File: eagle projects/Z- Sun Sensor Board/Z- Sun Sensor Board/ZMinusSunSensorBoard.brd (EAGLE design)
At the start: 78 x 78 mm, 53 parts, among them U2 ADS7841E_2K5, U4 LM20BIM7X_NOPB, U6 TLV9051IDCKR, U8 TLV9051IDCKR, U9 TLV9051IDCKR

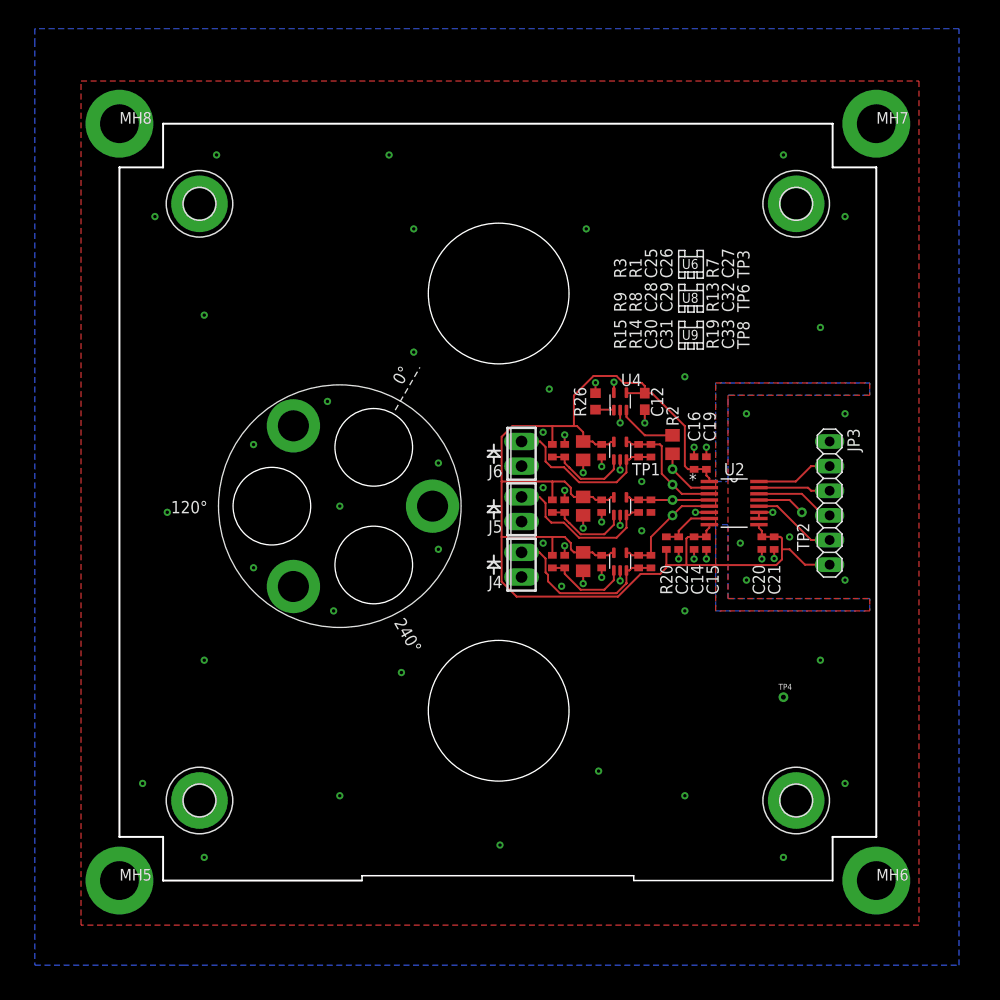
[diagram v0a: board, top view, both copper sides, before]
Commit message: Added mounting holes for sun sensor board, added standoff mounting holes to sensor board
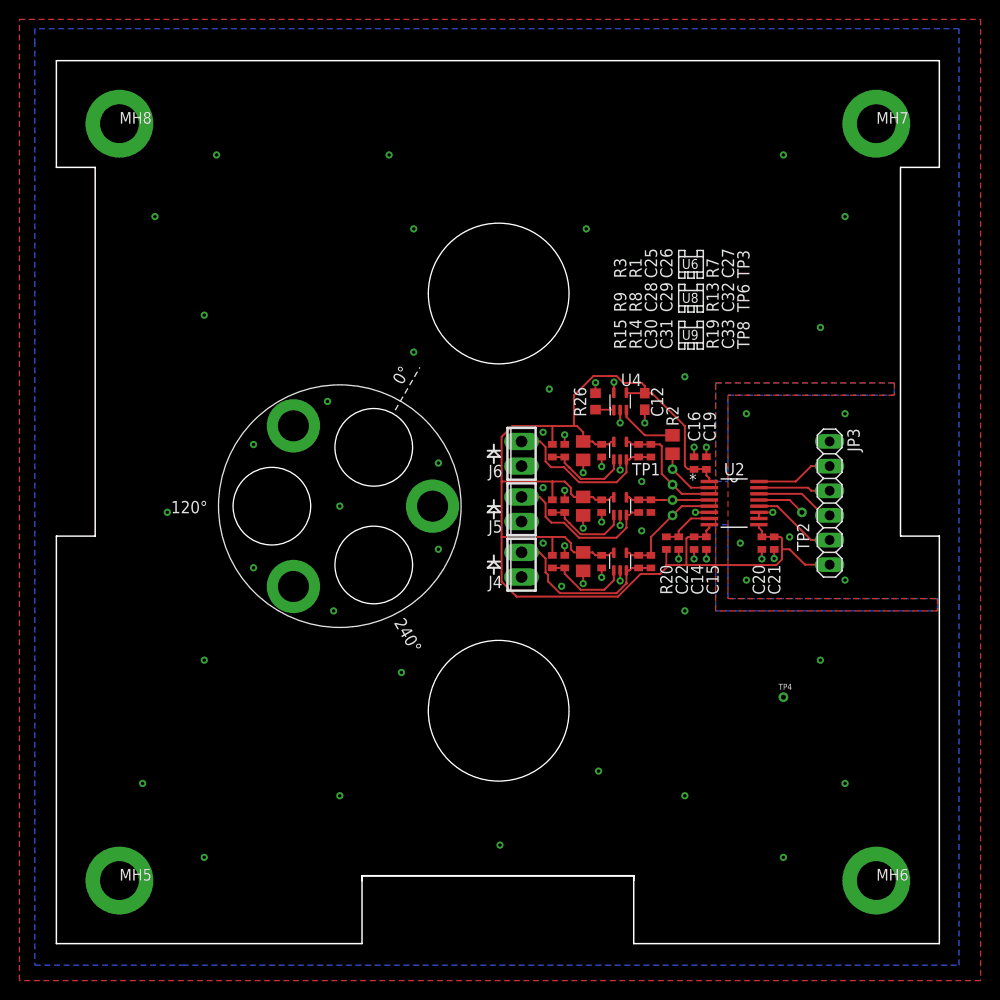
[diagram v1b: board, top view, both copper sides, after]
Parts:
- removed H1, H2, H3, H4: MOUNT-PAD-ROUND3.2, holes:3,2-PAD
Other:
- board size 78 x 78 mm -> 91 x 91 mm
- board text added: "Z- SUN SENSOR BOARD - Rev A"
- board text removed: "Z+ SUN SENSOR BOARD - Rev A"
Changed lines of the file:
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@@
 <setting verticaltext="up"/>
 </settings>
-<grid distance="25" unitdist="mil" unit="mil" style="lines" multiple="1" display="yes" altdistance="12.5" altunitdist="mil" altunit="mil"/>
+<grid distance="25" unitdist="mil" unit="mm" style="lines" multiple="1" display="yes" altdistance="12.5" altunitdist="mil" altunit="mil"/>
 <layers>
 <layer number="1" name="Top" color="4" fill="1" visible="yes" active="yes"/>
@@
 </layers>
 <board>
-<fusionsync huburn="a.YnVzaW5lc3M6bXlkYWwyMA" projecturn="a.YnVzaW5lc3M6bXlkYWwyMCMyMDE5MDkwNjIxMzMzMjg1MQ" f3durn="urn:adsk.wipprod:dm.lineage:9eKYqUHQRJ-z_v29RI24zA" pcbguid="" lastpulledtime="" lastsyncedchangeguid="" latestrevisionid="e225897c-414a-45e0-9606-f7f44216a340" lastsyncedrevisionid="e225897c-414a-45e0-9606-f7f44216a340" lastboardhashguid="898b3bb0-e8cf-4f41-3e9a-b056dcb77d80" lastpushedtime="2020-10-26T20:08:05Z" linktopcb3d="true"/>
+<fusionsync huburn="a.YnVzaW5lc3M6bXlkYWwyMA" projecturn="a.YnVzaW5lc3M6bXlkYWwyMCMyMDE5MDkwNjIxMzMzMjg1MQ" f3durn="urn:adsk.wipprod:dm.lineage:9eKYqUHQRJ-z_v29RI24zA" pcbguid="" lastpulledtime="" lastsyncedchangeguid="" latestrevisionid="e225897c-414a-45e0-9606-f7f44216a340" lastsyncedrevisionid="e225897c-414a-45e0-9606-f7f44216a340" lastboardhashguid="898b3bb0-e8cf-4f41-3e9a-b056dcb77d80" lastpushedtime="2020-10-26T20:08:05Z" linktopcb3d="false"/>
 <plain>
 <dimension x1="154.94" y1="86.995" x2="154.94" y2="13.335" x3="148.336" y3="50.165" textsize="3.5" layer="47"/>
 <dimension x1="213.36" y1="86.995" x2="154.94" y2="86.995" x3="184.15" y3="90.1954" textsize="3.5" layer="47"/>
-<wire x1="0" y1="0" x2="31.5" y2="0" width="0.1524" layer="48"/>
-<wire x1="31.5" y1="0" x2="31.5" y2="7" width="0.1524" layer="48"/>
+<wire x1="0" y1="0" x2="31.5" y2="0" width="0.1524" layer="20"/>
+<wire x1="31.5" y1="0" x2="31.5" y2="7" width="0.1524" layer="20"/>
 <wire x1="31.5" y1="7" x2="59.5" y2="7" width="0.1524" layer="20"/>
-<wire x1="59.5" y1="7" x2="59.5" y2="0" width="0.1524" layer="48"/>
-<wire x1="59.5" y1="0" x2="91" y2="0" width="0.1524" layer="48"/>
-<wire x1="91" y1="0" x2="91" y2="42" width="0.1524" layer="48"/>
-<wire x1="91" y1="42" x2="87" y2="42" width="0.1524" layer="48"/>
-<wire x1="87" y1="42" x2="87" y2="80" width="0.1524" layer="48"/>
-<wire x1="87" y1="80" x2="91" y2="80" width="0.1524" layer="48"/>
-<wire x1="91" y1="80" x2="91" y2="91" width="0.1524" layer="48"/>
-<wire x1="91" y1="91" x2="0" y2="91" width="0.1524" layer="48"/>
-<wire x1="0" y1="91" x2="0" y2="80" width="0.1524" layer="48"/>
-<wire x1="0" y1="80" x2="4" y2="80" width="0.1524" layer="48"/>
-<wire x1="4" y1="80" x2="4" y2="42" width="0.1524" layer="48"/>
-<wire x1="4" y1="42" x2="0" y2="42" width="0.1524" layer="48"/>
-<wire x1="0" y1="42" x2="0" y2="0" width="0.1524" layer="48"/>
+<wire x1="59.5" y1="7" x2="59.5" y2="0" width="0.1524" layer="20"/>
+<wire x1="59.5" y1="0" x2="91" y2="0" width="0.1524" layer="20"/>
+<wire x1="91" y1="0" x2="91" y2="42" width="0.1524" layer="20"/>
+<wire x1="91" y1="42" x2="87" y2="42" width="0.1524" layer="20"/>
+<wire x1="87" y1="42" x2="87" y2="80" width="0.1524" layer="20"/>
+<wire x1="87" y1="80" x2="91" y2="80" width="0.1524" layer="20"/>
+<wire x1="91" y1="80" x2="91" y2="91" width="0.1524" layer="20"/>
+<wire x1="91" y1="91" x2="0" y2="91" width="0.1524" layer="20"/>
+<wire x1="0" y1="91" x2="0" y2="80" width="0.1524" layer="20"/>
+<wire x1="0" y1="80" x2="4" y2="80" width="0.1524" layer="20"/>
+<wire x1="4" y1="80" x2="4" y2="42" width="0.1524" layer="20"/>
+<wire x1="4" y1="42" x2="0" y2="42" width="0.1524" layer="20"/>
+<wire x1="0" y1="42" x2="0" y2="0" width="0.1524" layer="20"/>
 <dimension x1="127" y1="89.535" x2="127" y2="15.875" x3="120.396" y3="52.705" textsize="3.5" layer="47"/>
 <dimension x1="185.42" y1="89.535" x2="127" y2="89.535" x3="156.21" y3="92.7354" textsize="3.5" layer="47"/>
 <text x="50.165" y="80.01" size="1.016" layer="51" rot="R180" align="bottom-right">Designed by T. Christison</text>
-<text x="50.165" y="81.28" size="1.016" layer="51" rot="R180" align="bottom-right">Z+ SUN SENSOR BOARD - Rev A</text>
+<text x="50.165" y="81.28" size="1.016" layer="51" rot="R180" align="bottom-right">Z- SUN SENSOR BOARD - Rev A</text>
 <text x="50.165" y="77.47" size="1.016" layer="151">Dalhousie Space Systems Lab</text>
 <hole x="45.5828" y="67" drill="14.5" locked="yes"/>
 <hole x="45.5828" y="24" drill="14.5" locked="yes"/>
-<wire x1="6.5" y1="11" x2="6.5" y2="80" width="0.2032" layer="20"/>
-<wire x1="6.5" y1="80" x2="11" y2="80" width="0.2032" layer="20"/>
-<wire x1="11" y1="84.5" x2="11" y2="80" width="0.2032" layer="20"/>
-<wire x1="11" y1="84.5" x2="80" y2="84.5" width="0.2032" layer="20"/>
-<wire x1="80" y1="84.5" x2="80" y2="80" width="0.2032" layer="20"/>
-<wire x1="80" y1="80" x2="84.5" y2="80" width="0.2032" layer="20"/>
-<wire x1="84.5" y1="80" x2="84.5" y2="11" width="0.2032" layer="20"/>
-<wire x1="84.5" y1="11" x2="80" y2="11" width="0.2032" layer="20"/>
-<wire x1="80" y1="11" x2="80" y2="6.5" width="0.2032" layer="20"/>
-<wire x1="31.5" y1="6.5" x2="11" y2="6.5" width="0.2032" layer="20"/>
-<wire x1="11" y1="6.5" x2="11" y2="11" width="0.2032" layer="20"/>
-<wire x1="11" y1="11" x2="6.5" y2="11" width="0.2032" layer="20"/>
 <wire x1="45.085" y1="39.37" x2="44.45" y2="39.37" width="0.2032" layer="21"/>
 <wire x1="45.085" y1="39.37" x2="45.72" y2="39.37" width="0.2032" layer="21"/>
@@
 <wire x1="45.085" y1="50.165" x2="45.085" y2="49.53" width="0.2032" layer="21"/>
 <wire x1="45.085" y1="50.8" x2="45.085" y2="51.435" width="0.2032" layer="21"/>
-<wire x1="31.5" y1="7" x2="59.5" y2="7" width="0.1524" layer="48"/>
+<wire x1="31.5" y1="7" x2="59.5" y2="7" width="0.1524" layer="20"/>
 <wire x1="31.5" y1="6.5" x2="31.5" y2="7" width="0.1524" layer="20"/>
 <wire x1="59.5" y1="6.5" x2="59.5" y2="7" width="0.1524" layer="20"/>
-<wire x1="59.5" y1="6.5" x2="80" y2="6.5" width="0.1524" layer="20"/>
 <text x="64.462659375" y="62.23508125" size="1.016" layer="21">U9</text>
 <wire x1="64.135" y1="63.5" x2="64.77" y2="63.5" width="0.1524" layer="21"/>
@@
 <attribute name="VALUE" x="76.5175" y="53.0225" size="1.27" layer="27" rot="R270"/>
 </element>
-<element name="H1" library="holes" library_urn="urn:adsk.eagle:library:237" package="3,2-PAD" package3d_urn="urn:adsk.eagle:package:14282/1" value="MOUNT-PAD-ROUND3.2" x="14.75" y="76.245" locked="yes" smashed="yes">
-<attribute name="POPULARITY" value="4" x="14.75" y="76.245" locked="yes" size="1.778" layer="27" display="off"/>
-</element>
-<element name="H2" library="holes" library_urn="urn:adsk.eagle:library:237" package="3,2-PAD" package3d_urn="urn:adsk.eagle:package:14282/1" value="MOUNT-PAD-ROUND3.2" x="14.75" y="14.75" locked="yes" smashed="yes">
-<attribute name="POPULARITY" value="4" x="14.75" y="14.75" locked="yes" size="1.778" layer="27" display="off"/>
-</element>
-<element name="H3" library="holes" library_urn="urn:adsk.eagle:library:237" package="3,2-PAD" package3d_urn="urn:adsk.eagle:package:14282/1" value="MOUNT-PAD-ROUND3.2" x="76.245" y="14.75" locked="yes" smashed="yes">
-<attribute name="POPULARITY" value="4" x="76.245" y="14.75" locked="yes" size="1.778" layer="27" display="off"/>
-</element>
-<element name="H4" library="holes" library_urn="urn:adsk.eagle:library:237" package="3,2-PAD" package3d_urn="urn:adsk.eagle:package:14282/1" value="MOUNT-PAD-ROUND3.2" x="76.245" y="76.245" locked="yes" smashed="yes">
-<attribute name="POPULARITY" value="4" x="76.245" y="76.245" locked="yes" size="1.778" layer="27" display="off"/>
-</element>
 <element name="TP4" library="my_library" library_urn="urn:adsk.eagle:library:22876504" package="TP_P76H50" package3d_urn="urn:adsk.eagle:package:24605432/2" value="TESTPOINT" x="74.93" y="25.4" smashed="yes">
 <attribute name="NAME" x="74.422" y="26.162" size="0.6096" layer="25" font="vector" ratio="10"/>
@@
 <wire x1="65.7225" y1="39.6444" x2="65.7225" y2="40.625" width="0.2032" layer="1"/>
 <contactref element="JP3" pad="1"/>
-<polygon width="0.2032" layer="1">
-<vertex x="2.54" y="88.9"/>
-<vertex x="88.9" y="88.9"/>
-<vertex x="88.9" y="1.905"/>
-<vertex x="2.54" y="1.905"/>
-</polygon>
 <polygon width="0.2032" layer="1" pour="cutout">
-<vertex x="67.945" y="36.195"/>
+<vertex x="67.945" y="34.29"/>
 <vertex x="67.945" y="57.785"/>
-<vertex x="83.82" y="57.785"/>
-<vertex x="83.82" y="56.515"/>
+<vertex x="86.36" y="57.785"/>
+<vertex x="86.36" y="56.515"/>
 <vertex x="69.215" y="56.515"/>
-<vertex x="69.215" y="55.88"/>
 <vertex x="69.215" y="35.56"/>
-<vertex x="83.82" y="35.56"/>
-<vertex x="83.82" y="34.29"/>
-<vertex x="67.945" y="34.29"/>
+<vertex x="90.805" y="35.56"/>
+<vertex x="90.805" y="34.29"/>
 </polygon>
 <polygon width="0.2032" layer="16" pour="cutout">
@@
 <vertex x="69.215" y="47.625"/>
 <vertex x="69.215" y="56.515"/>
-<vertex x="83.82" y="56.515"/>
-<vertex x="83.82" y="57.785"/>
+<vertex x="86.36" y="56.515"/>
+<vertex x="86.36" y="57.785"/>
 <vertex x="67.945" y="57.785"/>
 </polygon>
 <polygon width="0.2032" layer="16" pour="cutout">
-<vertex x="83.82" y="35.56"/>
+<vertex x="90.805" y="35.56"/>
 <vertex x="69.215" y="35.56"/>
 <vertex x="69.215" y="43.18"/>
 <vertex x="67.945" y="43.18"/>
 <vertex x="67.945" y="34.29"/>
-<vertex x="83.82" y="34.29"/>
+<vertex x="90.805" y="34.29"/>
 </polygon>
 <via x="71.12" y="54.61" extent="1-16" drill="0.35"/>
@@
 <via x="52.07" y="36.83" extent="1-16" drill="0.35"/>
 <contactref element="TP4" pad="1"/>
+<polygon width="0.1524" layer="1">
+<vertex x="-3.81" y="95.25"/>
+<vertex x="95.25" y="95.25"/>
+<vertex x="95.25" y="-3.81"/>
+<vertex x="-3.81" y="-3.81"/>
+<vertex x="-3.81" y="-1.905"/>
+</polygon>
 </signal>
 <signal name="UCB0_SPI_CLK">

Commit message: Small value updates, new titleblock, and added bom
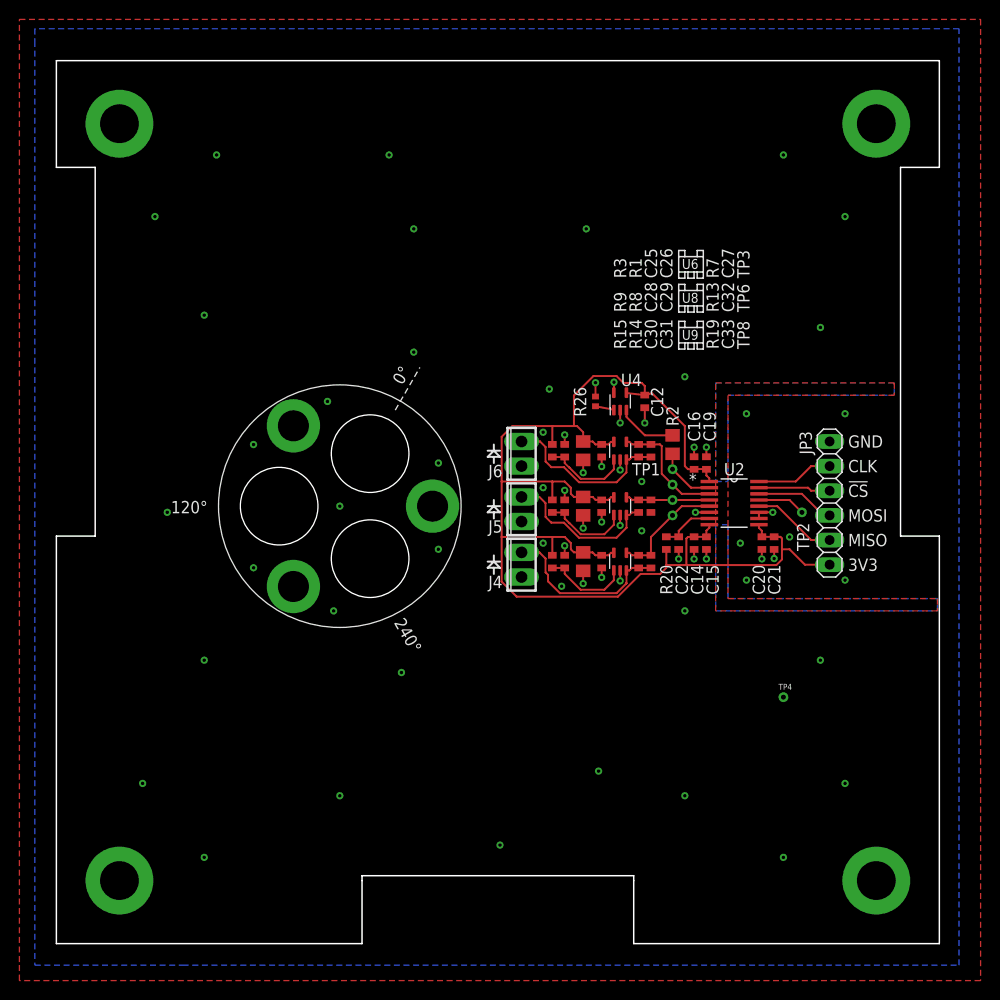
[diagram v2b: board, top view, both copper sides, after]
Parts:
- C12: device rcl:C0603 -> rcl:C0402
- C27, C32, C33: value 0.015u -> 0.022u
- R13, R19, R7: value 5.6k -> 3.74k
- R26: device rcl:R0603 -> rcl:R0402
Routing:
- net GND: track 28.2 -> 28.8 mm
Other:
- board text added: "!CS"
- board text added: "3V3"
- board text added: "CLK"
- board text added: "GND"
- board text added: "MISO"
- board text added: "MOSI"
